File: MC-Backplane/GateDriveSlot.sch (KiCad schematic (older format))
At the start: 1 part, among them U6 86094328314755V1LF

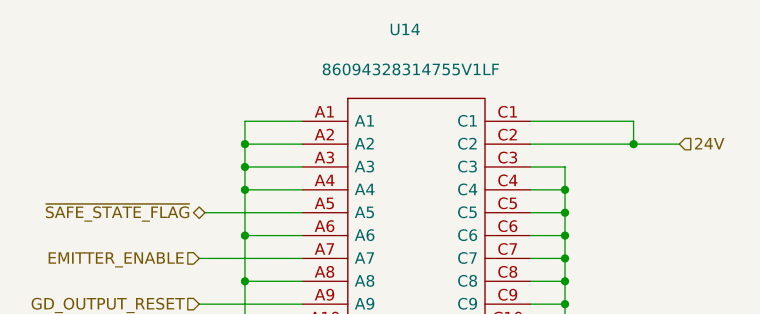
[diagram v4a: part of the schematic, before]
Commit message: removed some MHs and attempted to fix library
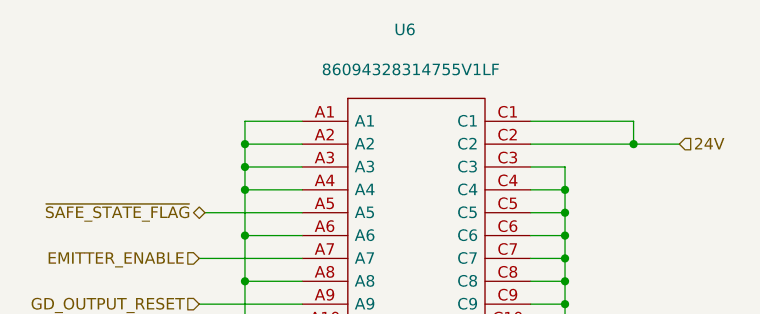
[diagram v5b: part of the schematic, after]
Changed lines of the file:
@@
 AR Path="/6245C75C/6229BF81" Ref="U8"  Part="1"
 AR Path="/6245C76A/6229BF81" Ref="U9"  Part="1"
-F 0 "U14" H 5375 2900 50  0000 C CNN
+F 0 "U6" H 5375 2900 50  0000 C CNN
 F 1 "86094328314755V1LF" H 5400 2725 50  0000 C CNN
 F 2 "Footprints_MC-Backplane:86094328314755V1LF" H 4925 2500 50  0001 C CNN
